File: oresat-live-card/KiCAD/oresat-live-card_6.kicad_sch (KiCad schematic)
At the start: 40 parts, among them J2 SM06B-SRSS-TB(LF)(SN), J5 2X1_TH_JUMPEP, J9 U.FL-R-SMA, U19 TQP9111, U6 SN74LVC1G32QDBVRQ1, U8 MIC94090YC6-TR

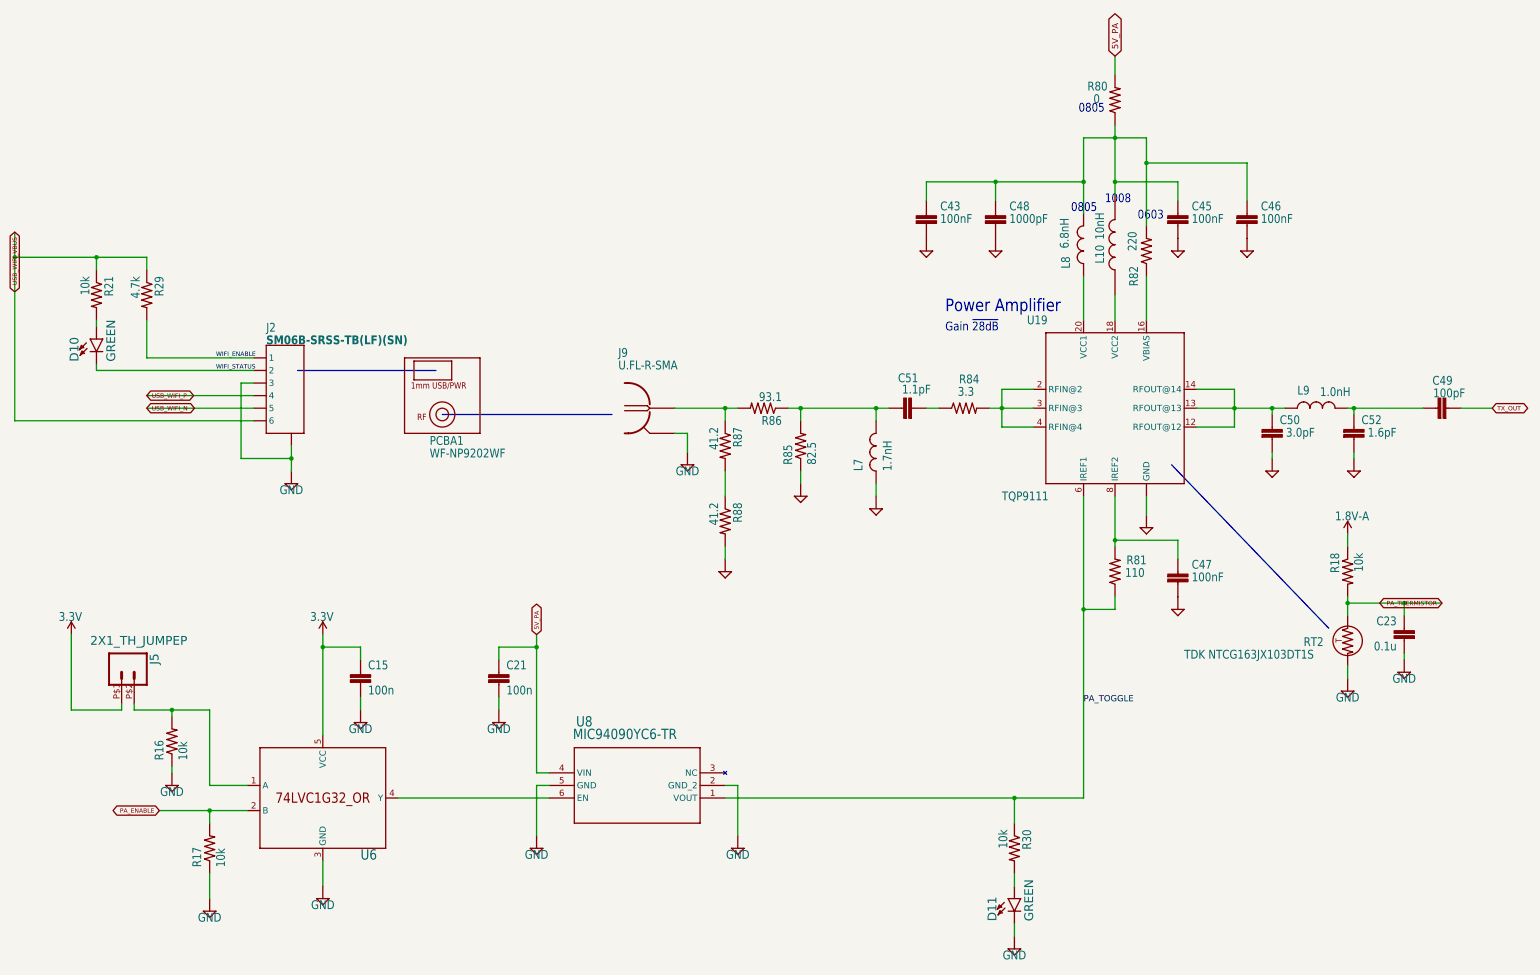
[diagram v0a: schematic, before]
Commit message: BOM and minor cosmetic schematic updates
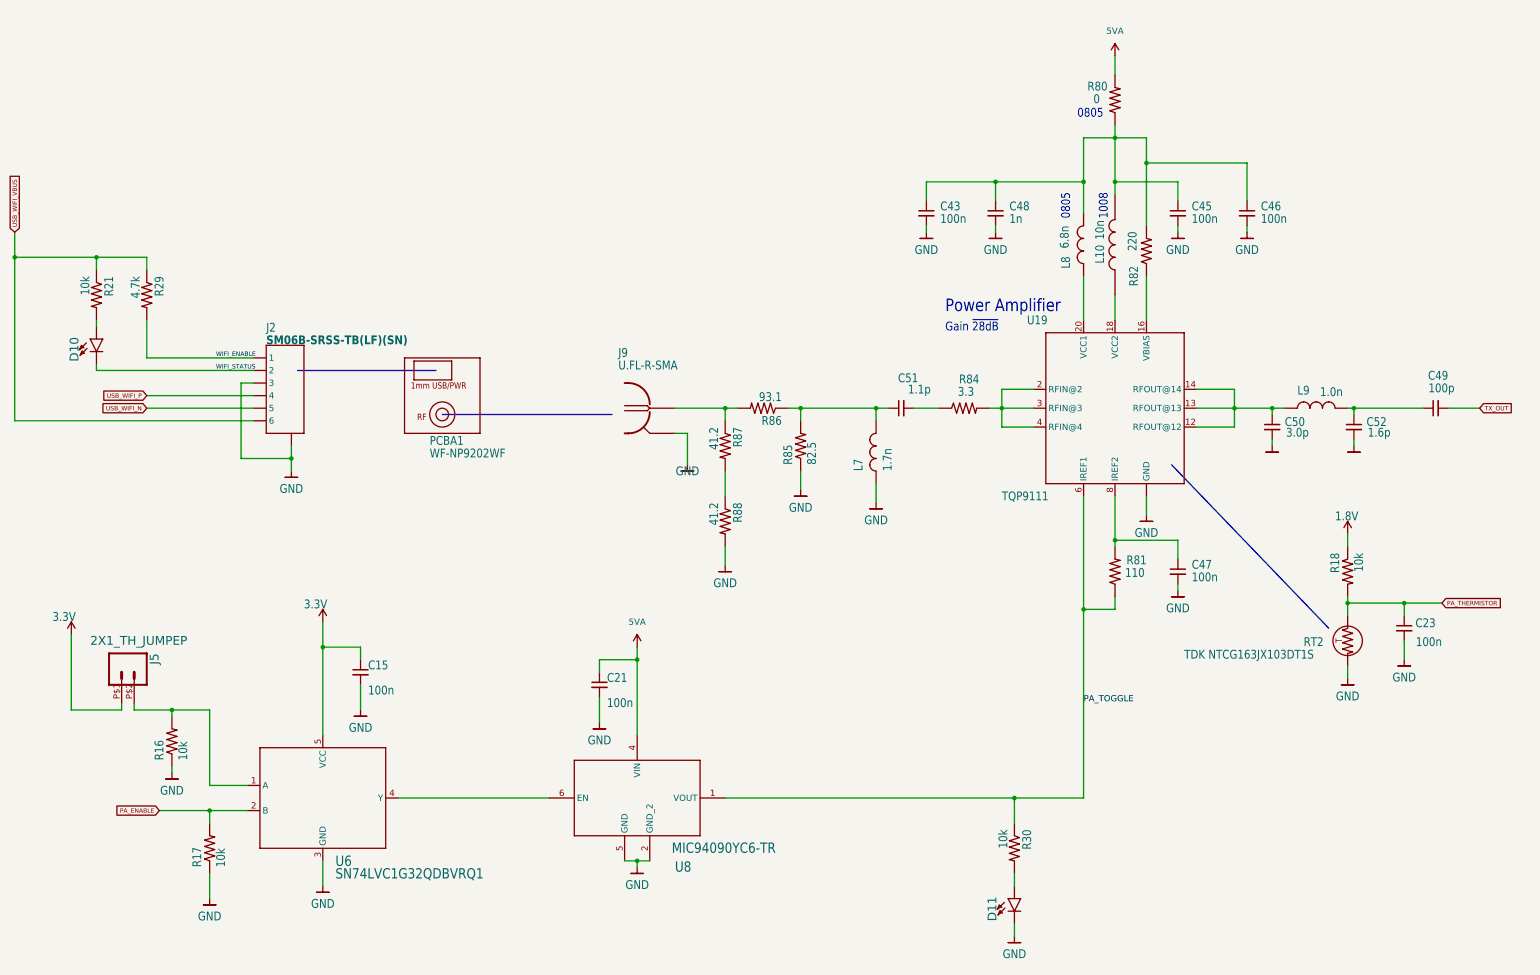
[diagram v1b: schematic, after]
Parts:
- C15, C21: footprint oresat-live-card:.0603-A -> Resistor_SMD:R_0603_1608Metric; symbol oresat-live-card-eagle-import:C-EU0603-A -> Device:C_Small; Distributor (none) -> DigiKey; MPN (none) -> CL10B104KB8WPNC
- C23: value 0.1u -> 100n; footprint oresat-live-card:.0603-A -> Resistor_SMD:R_0603_1608Metric; symbol oresat-live-card-eagle-import:C-EU0603-A -> Device:C_Small; Distributor (none) -> DigiKey; MPN (none) -> CL10B104KB8WPNC
- C43, C45, C46: symbol oresat-live-card-eagle-import:C-EU0402-B-NOSILK -> Device:C_Small; Distributor (none) -> DigiKey; MPN (none) -> CGJ2B3X7R1E104K050BB
- C47: footprint oresat-live-card:.0402-C-NOSILK -> oresat-live-card:.0402-B-NOSILK; symbol oresat-live-card-eagle-import:C-EU0402-C-NOSILK -> Device:C_Small; Distributor (none) -> DigiKey; MPN (none) -> CGJ2B3X7R1E104K050BB
- C48: symbol oresat-live-card-eagle-import:C-EU0402-B-NOSILK -> Device:C_Small; Distributor (none) -> DigiKey; MPN (none) -> TMF105B7102KVHF
- C49: symbol oresat-live-card-eagle-import:C-EU0402-C-NOSILK -> Device:C_Small; Distributor (none) -> DigiKey; MPN (none) -> C0402C101K4RACAUTO
- C50: symbol oresat-live-card-eagle-import:C-EU0402-C-NOSILK -> Device:C_Small; Distributor (none) -> DigiKey; MPN (none) -> 04025U3R0BAT2A
- C51: symbol oresat-live-card-eagle-import:C-EU0402-C-NOSILK -> Device:C_Small; Distributor (none) -> DigiKey; MPN (none) -> 04025J1R1PBSTR\500
- C52: symbol oresat-live-card-eagle-import:C-EU0402-C-NOSILK -> Device:C_Small; Distributor (none) -> DigiKey; MPN (none) -> 04025U1R6BAT2A
- D10, D11: Distributor (none) -> DigiKey; MPN (none) -> 150060GS75020
- J2: Distributor (none) -> DigiKey; MPN (none) -> SM06B-SRSS-TB(LF)(SN)
- J9: Distributor (none) -> DigiKey; MPN (none) -> U.FL-R-SMT-1(10)
- L10: Distributor (none) -> DigiKey; MPN (none) -> 1008HQ-10NXJLB
- L7: Distributor (none) -> DigiKey; MPN (none) -> 0402DC-1N7XJRU
- L8: Distributor (none) -> DigiKey; MPN (none) -> 0805CS-060XJLC
- L9: Distributor (none) -> DigiKey; MPN (none) -> MLK1005S1N0ST000
- R16, R17, R18, R21, R30: footprint oresat-live-card:.0603-A -> Resistor_SMD:R_0603_1608Metric; Distributor (none) -> DigiKey; MPN (none) -> ERJ-3EKF1002V
- R29: footprint oresat-live-card:.0603-A -> Resistor_SMD:R_0603_1608Metric; Distributor (none) -> DigiKey; MPN (none) -> ERJ-3EKF4701V
- R80: Distributor (none) -> DigiKey; MPN (none) -> ERJ-6GEY0R00V
- R81: Distributor (none) -> DigiKey; MPN (none) -> ERJ-2RKF1100X
- R82: Distributor (none) -> DigiKey; MPN (none) -> ERJ-3EKF2200V
- R84: Distributor (none) -> DigiKey; MPN (none) -> CRCW04023R30FKED
- R85: footprint oresat-live-card:.0603-A -> Resistor_SMD:R_0603_1608Metric; Distributor (none) -> DigiKey; MPN (none) -> ERJ-3EKF82R5V
- R86: footprint oresat-live-card:.0603-A -> Resistor_SMD:R_0603_1608Metric; Distributor (none) -> DigiKey; MPN (none) -> ERJ-3EKF93R1V
- R87, R88: footprint oresat-live-card:.0603-A -> Resistor_SMD:R_0603_1608Metric; Distributor (none) -> DigiKey; MPN (none) -> ERJ-3EKF41R2V
- RT2: Distributor (none) -> DigiKey; MPN (none) -> NTCG163JX103DT1S
- U19: Distributor (none) -> DigiKey; MPN (none) -> TQP9111
- U6: Distributor (none) -> DigiKey; MPN (none) -> SN74LVC1G32QDBVRQ1
- U8: Distributor (none) -> DigiKey; MPN (none) -> MIC94090YC6
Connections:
- net 3.3V is gone; now on net PWR: C15.1, J5.P$1 (1), U6.5 (VCC)
- net 5V_PA is gone; now on net PWR: C21.1, R80.2, U8.4 (VIN)
- net 1.8V-A renamed PWR
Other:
- note removed: "0603"

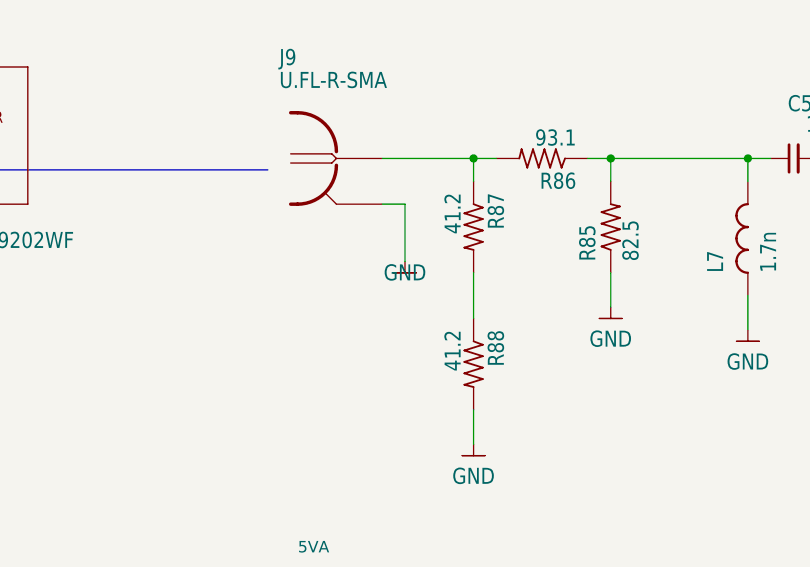
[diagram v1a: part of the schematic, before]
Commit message: updated schematic with new 5.5V reg
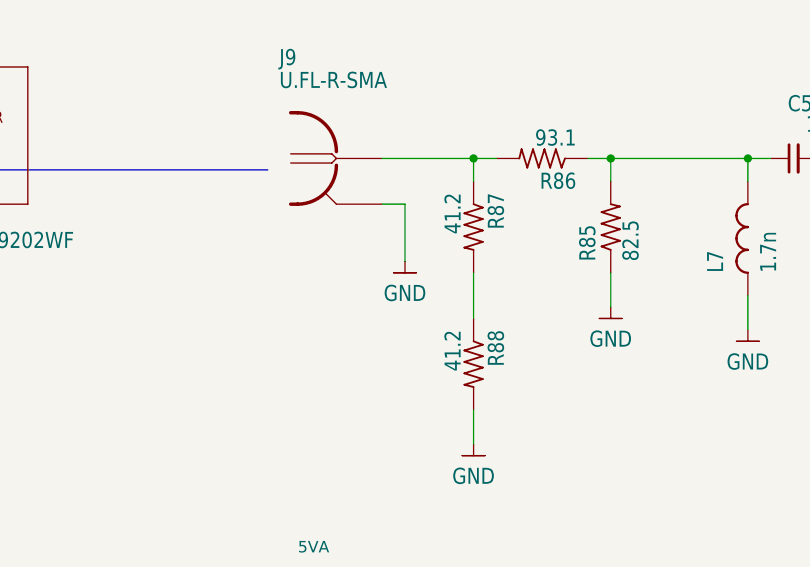
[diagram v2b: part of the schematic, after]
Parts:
- C43, C45, C46, C47: footprint oresat-live-card:.0402-B-NOSILK -> Resistor_SMD:R_0603_1608Metric; MPN CGJ2B3X7R1E104K050BB -> CL10B104KB8WPNC
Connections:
- removed net PWR: C15.1, C21.1, J5.P$1 (1), R18.1, R80.2, U6.5 (VCC), U8.4 (VIN)
- new net 1.8V: R18.1
- new net 3.3V: C15.1, J5.P$1 (1), U6.5 (VCC)
- new net 5VA: C21.1, R80.2, U8.4 (VIN)
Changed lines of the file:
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@@
       (effects (font (size 1.27 1.27)) hide)
     )
-    (property "Value" "GND" (id 1) (at 167.64 125.984 0)
+    (property "Value" "GND" (id 1) (at 167.64 128.27 0)
       (effects (font (size 1.778 1.5113)) (justify top))
     )
@@
       (effects (font (size 1.778 1.5113)) (justify left bottom))
     )
-    (property "Footprint" "oresat-live-card:.0402-B-NOSILK" (id 2) (at 266.7 74.93 0)
+    (property "Footprint" "Resistor_SMD:R_0603_1608Metric" (id 2) (at 266.7 74.93 0)
       (effects (font (size 1.27 1.27)) hide)
     )
@@
       (effects (font (size 1.778 1.5113)) (justify left bottom) hide)
     )
-    (property "Description" "0.1 µF ±10% 25V Ceramic Capacitor X7R 0402 (1005 Metric)" (id 5) (at 266.7 74.93 0)
+    (property "Description" "0.1 µF ±10% 50V Ceramic Capacitor X7R 0603 (1608 Metric)" (id 5) (at 266.7 74.93 0)
       (effects (font (size 1.27 1.27)) hide)
     )
@@
       (effects (font (size 1.27 1.27)) hide)
     )
-    (property "MPN" "CGJ2B3X7R1E104K050BB" (id 7) (at 266.7 74.93 0)
+    (property "MPN" "CL10B104KB8WPNC" (id 7) (at 266.7 74.93 0)
       (effects (font (size 1.27 1.27)) hide)
     )
@@
       (effects (font (size 1.778 1.5113)) (justify left bottom))
     )
-    (property "Footprint" "oresat-live-card:.0402-B-NOSILK" (id 2) (at 215.9 74.93 0)
+    (property "Footprint" "Resistor_SMD:R_0603_1608Metric" (id 2) (at 215.9 74.93 0)
       (effects (font (size 1.27 1.27)) hide)
     )
@@
       (effects (font (size 1.778 1.5113)) (justify left bottom) hide)
     )
-    (property "Description" "0.1 µF ±10% 25V Ceramic Capacitor X7R 0402 (1005 Metric)" (id 5) (at 215.9 74.93 0)
+    (property "Description" "0.1 µF ±10% 50V Ceramic Capacitor X7R 0603 (1608 Metric)" (id 5) (at 215.9 74.93 0)
       (effects (font (size 1.27 1.27)) hide)
     )
@@
       (effects (font (size 1.27 1.27)) hide)
     )
-    (property "MPN" "CGJ2B3X7R1E104K050BB" (id 7) (at 215.9 74.93 0)
+    (property "MPN" "CL10B104KB8WPNC" (id 7) (at 215.9 74.93 0)
       (effects (font (size 1.27 1.27)) hide)
     )
@@
       (effects (font (size 1.778 1.5113)) (justify left bottom))
     )
-    (property "Footprint" "oresat-live-card:.0402-B-NOSILK" (id 2) (at 266.7 147.32 0)
+    (property "Footprint" "Resistor_SMD:R_0603_1608Metric" (id 2) (at 266.7 147.32 0)
       (effects (font (size 1.27 1.27)) hide)
     )
@@
       (effects (font (size 1.778 1.5113)) (justify left bottom) hide)
     )
-    (property "Description" "0.1 µF ±10% 25V Ceramic Capacitor X7R 0402 (1005 Metric)" (id 5) (at 266.7 147.32 0)
+    (property "Description" "0.1 µF ±10% 50V Ceramic Capacitor X7R 0603 (1608 Metric)" (id 5) (at 266.7 147.32 0)
       (effects (font (size 1.27 1.27)) hide)
     )
@@
       (effects (font (size 1.27 1.27)) hide)
     )
-    (property "MPN" "CGJ2B3X7R1E104K050BB" (id 7) (at 266.7 147.32 0)
+    (property "MPN" "CL10B104KB8WPNC" (id 7) (at 266.7 147.32 0)
       (effects (font (size 1.27 1.27)) hide)
     )
@@
   (symbol (lib_id "OreSat-Power:3.3V") (at 43.18 160.02 0) (unit 1)
     (in_bom yes) (on_board yes)
-    (property "Reference" "#3.3V02" (id 0) (at 43.18 160.02 0)
+    (property "Reference" "#3V0102" (id 0) (at 43.18 160.02 0)
       (effects (font (size 1.27 1.27)) hide)
     )
@@
   (symbol (lib_id "OreSat-Power:5VA") (at 157.48 162.56 0) (unit 1)
     (in_bom yes) (on_board yes) (fields_autoplaced)
-    (property "Reference" "#PWR02" (id 0) (at 157.48 166.37 0)
+    (property "Reference" "#5VA01" (id 0) (at 157.48 166.37 0)
       (effects (font (size 1.27 1.27)) hide)
     )
@@
   (symbol (lib_id "OreSat-Power:1.8V") (at 300.99 139.7 0) (unit 1)
     (in_bom yes) (on_board yes)
-    (property "Reference" "#1.8V-A03" (id 0) (at 300.99 139.7 0)
+    (property "Reference" "#1V0101" (id 0) (at 300.99 139.7 0)
       (effects (font (size 1.27 1.27)) hide)
     )
@@
     (pin "1")
   )
-  (symbol (lib_id "OreSat-Power:3.3V") (at 93.98 157.48 0) (unit 1)
-    (in_bom yes) (on_board yes)
-    (property "Reference" "#3.3V01" (id 0) (at 93.98 157.48 0)
+  (symbol (lib_name "3.3V_1") (lib_id "OreSat-Power:3.3V") (at 93.98 157.48 0) (unit 1)
+    (in_bom yes) (on_board yes)
+    (property "Reference" "#3V0101" (id 0) (at 93.98 157.48 0)
       (effects (font (size 1.27 1.27)) hide)
     )
@@
       (effects (font (size 1.778 1.5113)) (justify left bottom))
     )
-    (property "Footprint" "oresat-live-card:.0402-B-NOSILK" (id 2) (at 280.67 74.93 0)
+    (property "Footprint" "Resistor_SMD:R_0603_1608Metric" (id 2) (at 280.67 74.93 0)
       (effects (font (size 1.27 1.27)) hide)
     )
@@
       (effects (font (size 1.778 1.5113)) (justify left bottom) hide)
     )
-    (property "Description" "0.1 µF ±10% 25V Ceramic Capacitor X7R 0402 (1005 Metric)" (id 5) (at 280.67 74.93 0)
+    (property "Description" "0.1 µF ±10% 50V Ceramic Capacitor X7R 0603 (1608 Metric)" (id 5) (at 280.67 74.93 0)
       (effects (font (size 1.27 1.27)) hide)
     )
@@
       (effects (font (size 1.27 1.27)) hide)
     )
-    (property "MPN" "CGJ2B3X7R1E104K050BB" (id 7) (at 280.67 74.93 0)
+    (property "MPN" "CL10B104KB8WPNC" (id 7) (at 280.67 74.93 0)
       (effects (font (size 1.27 1.27)) hide)
     )
@@
     )
   )
-  (symbol (lib_id "OreSat-Power:5VA") (at 254 43.18 0) (unit 1)
+  (symbol (lib_name "5VA_1") (lib_id "OreSat-Power:5VA") (at 254 43.18 0) (unit 1)
     (in_bom yes) (on_board yes) (fields_autoplaced)
-    (property "Reference" "#PWR03" (id 0) (at 254 46.99 0)
-      (effects (font (size 1.27 1.27)) hide)
-    )
+    (property "Reference" "#5VA02" (id 0) (at 254 46.99 0)
+      (effects (font (size 1.27 1.27)) hide)
+    )
